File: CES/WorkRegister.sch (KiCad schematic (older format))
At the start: 12 parts, among them U401 RT1, U402 RT2, U403 RT3, U404 RT4, U405 BT1, U406 BT2

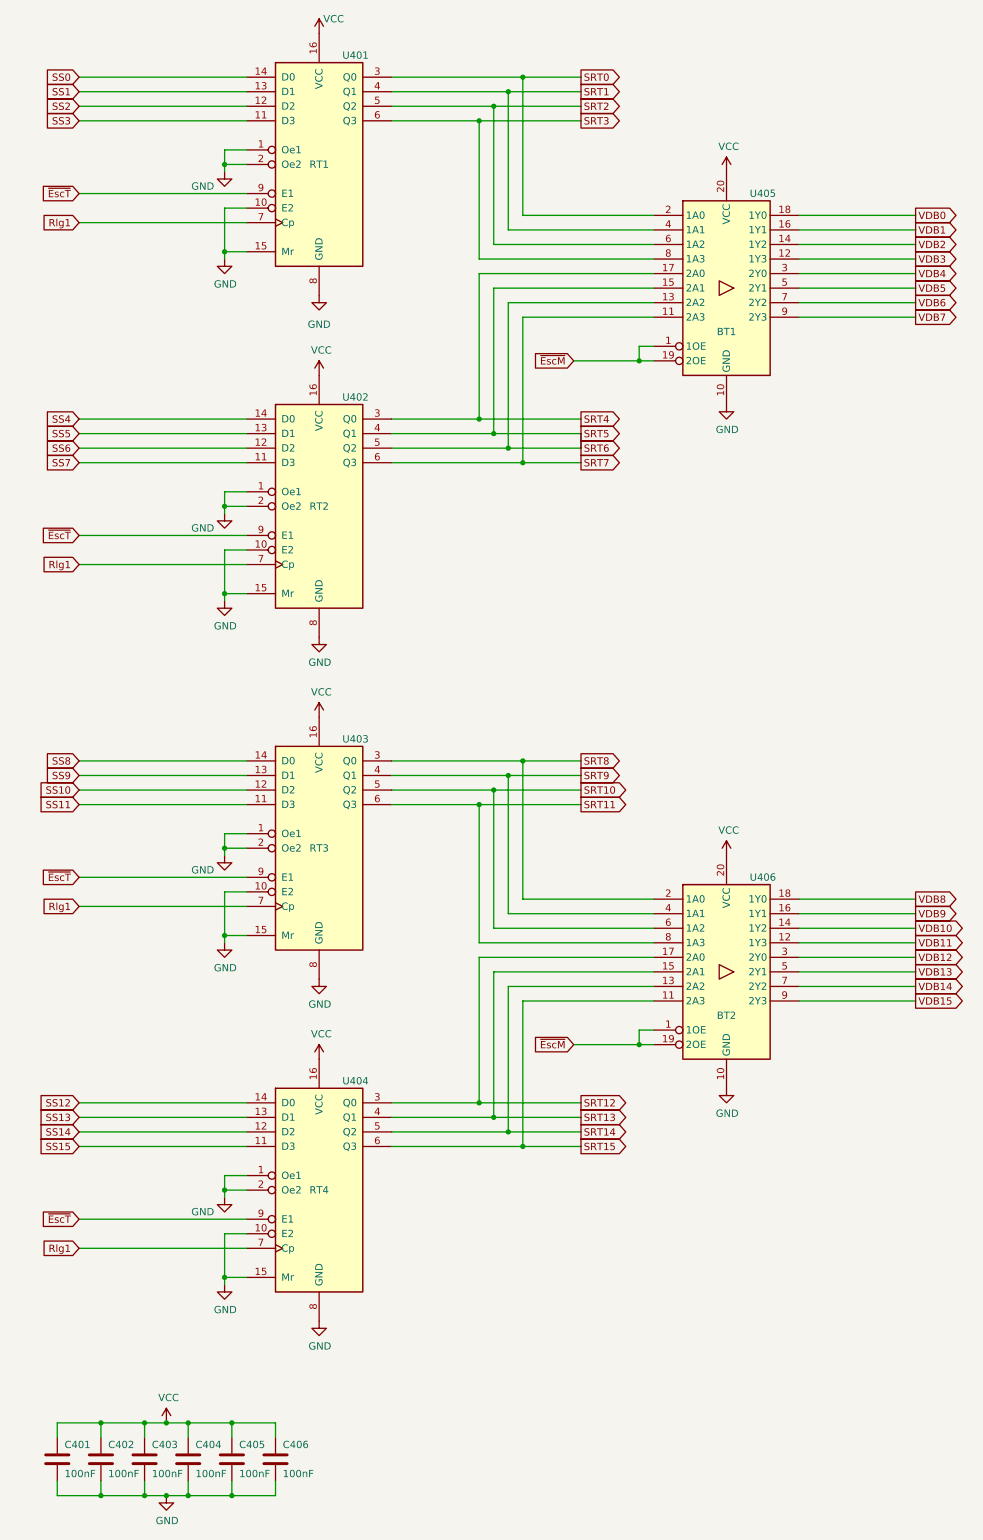
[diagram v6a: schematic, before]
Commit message: Correcting footprints errors
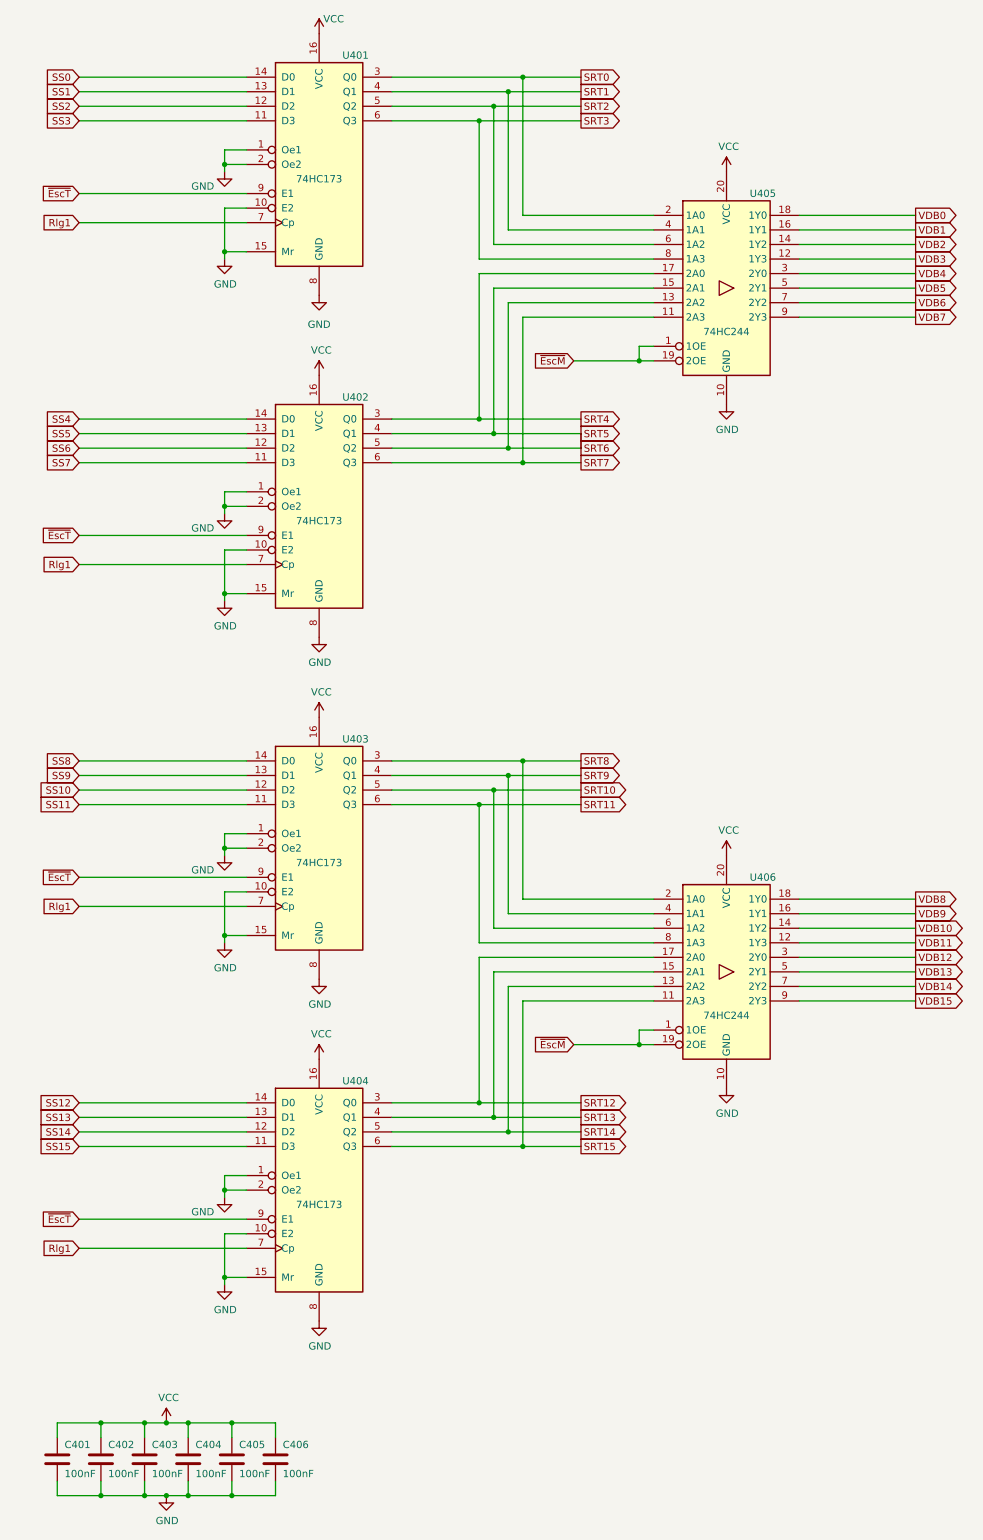
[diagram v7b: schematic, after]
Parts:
- C401, C402, C403, C404, C405, C406: footprint Capacitor_THT:CP_Radial_D5.0mm_P2.50mm -> Capacitor_THT:C_Disc_D4.3mm_W1.9mm_P5.00mm
- U401: value RT1 -> 74HC173
- U402: value RT2 -> 74HC173
- U403: value RT3 -> 74HC173
- U404: value RT4 -> 74HC173
- U405: value BT1 -> 74HC244
- U406: value BT2 -> 74HC244
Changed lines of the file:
@@
 P 5600 2450
 F 0 "U405" H 5850 3100 50  0000 C CNN
-F 1 "BT1" H 5600 2150 50  0000 C CNN
+F 1 "74HC244" H 5600 2150 50  0000 C CNN
 F 2 "Package_DIP:DIP-20_W7.62mm" H 5600 2450 50  0001 C CNN
 F 3 "https://assets.nexperia.com/documents/data-sheet/74HC_HCT244.pdf" H 5600 2450 50  0001 C CNN
@@
 P 5600 7150
 F 0 "U406" H 5850 7800 50  0000 C CNN
-F 1 "BT2" H 5600 6850 50  0000 C CNN
+F 1 "74HC244" H 5600 6850 50  0000 C CNN
 F 2 "Package_DIP:DIP-20_W7.62mm" H 5600 7150 50  0001 C CNN
 F 3 "https://assets.nexperia.com/documents/data-sheet/74HC_HCT244.pdf" H 5600 7150 50  0001 C CNN
@@
 F 0 "C401" H 1050 10600 50  0000 L CNN
 F 1 "100nF" H 1050 10400 50  0000 L CNN
-F 2 "Capacitor_THT:CP_Radial_D5.0mm_P2.50mm" H 1038 10350 50  0001 C CNN
+F 2 "Capacitor_THT:C_Disc_D4.3mm_W1.9mm_P5.00mm" H 1038 10350 50  0001 C CNN
 F 3 "~" H 1000 10500 50  0001 C CNN
 	1    1000 10500
@@
 F 0 "C402" H 1350 10600 50  0000 L CNN
 F 1 "100nF" H 1350 10400 50  0000 L CNN
-F 2 "Capacitor_THT:CP_Radial_D5.0mm_P2.50mm" H 1338 10350 50  0001 C CNN
+F 2 "Capacitor_THT:C_Disc_D4.3mm_W1.9mm_P5.00mm" H 1338 10350 50  0001 C CNN
 F 3 "~" H 1300 10500 50  0001 C CNN
 	1    1300 10500
@@
 F 0 "C403" H 1650 10600 50  0000 L CNN
 F 1 "100nF" H 1650 10400 50  0000 L CNN
-F 2 "Capacitor_THT:CP_Radial_D5.0mm_P2.50mm" H 1638 10350 50  0001 C CNN
+F 2 "Capacitor_THT:C_Disc_D4.3mm_W1.9mm_P5.00mm" H 1638 10350 50  0001 C CNN
 F 3 "~" H 1600 10500 50  0001 C CNN
 	1    1600 10500
@@
 F 0 "C404" H 1950 10600 50  0000 L CNN
 F 1 "100nF" H 1950 10400 50  0000 L CNN
-F 2 "Capacitor_THT:CP_Radial_D5.0mm_P2.50mm" H 1938 10350 50  0001 C CNN
+F 2 "Capacitor_THT:C_Disc_D4.3mm_W1.9mm_P5.00mm" H 1938 10350 50  0001 C CNN
 F 3 "~" H 1900 10500 50  0001 C CNN
 	1    1900 10500
@@
 F 0 "C405" H 2250 10600 50  0000 L CNN
 F 1 "100nF" H 2250 10400 50  0000 L CNN
-F 2 "Capacitor_THT:CP_Radial_D5.0mm_P2.50mm" H 2238 10350 50  0001 C CNN
+F 2 "Capacitor_THT:C_Disc_D4.3mm_W1.9mm_P5.00mm" H 2238 10350 50  0001 C CNN
 F 3 "~" H 2200 10500 50  0001 C CNN
 	1    2200 10500
@@
 F 0 "C406" H 2550 10600 50  0000 L CNN
 F 1 "100nF" H 2550 10400 50  0000 L CNN
-F 2 "Capacitor_THT:CP_Radial_D5.0mm_P2.50mm" H 2538 10350 50  0001 C CNN
+F 2 "Capacitor_THT:C_Disc_D4.3mm_W1.9mm_P5.00mm" H 2538 10350 50  0001 C CNN
 F 3 "~" H 2500 10500 50  0001 C CNN
 	1    2500 10500
@@
 P 2800 1600
 F 0 "U401" H 3050 2350 50  0000 C CNN
-F 1 "RT1" H 2800 1600 50  0000 C CNN
+F 1 "74HC173" H 2800 1500 50  0000 C CNN
 F 2 "Package_DIP:DIP-16_W7.62mm" H 2800 1600 50  0001 C CNN
 F 3 "http://www.ti.com/lit/gpn/cd74HC173" H 2800 1600 50  0001 C CNN
@@
 P 2800 3950
 F 0 "U402" H 3050 4700 50  0000 C CNN
-F 1 "RT2" H 2800 3950 50  0000 C CNN
+F 1 "74HC173" H 2800 3850 50  0000 C CNN
 F 2 "Package_DIP:DIP-16_W7.62mm" H 2800 3950 50  0001 C CNN
 F 3 "http://www.ti.com/lit/gpn/cd74HC173" H 2800 3950 50  0001 C CNN
@@
 P 2800 6300
 F 0 "U403" H 3050 7050 50  0000 C CNN
-F 1 "RT3" H 2800 6300 50  0000 C CNN
+F 1 "74HC173" H 2800 6200 50  0000 C CNN
 F 2 "Package_DIP:DIP-16_W7.62mm" H 2800 6300 50  0001 C CNN
 F 3 "http://www.ti.com/lit/gpn/cd74HC173" H 2800 6300 50  0001 C CNN
@@
 P 2800 8650
 F 0 "U404" H 3050 9400 50  0000 C CNN
-F 1 "RT4" H 2800 8650 50  0000 C CNN
+F 1 "74HC173" H 2800 8550 50  0000 C CNN
 F 2 "Package_DIP:DIP-16_W7.62mm" H 2800 8650 50  0001 C CNN
 F 3 "http://www.ti.com/lit/gpn/cd74HC173" H 2800 8650 50  0001 C CNN

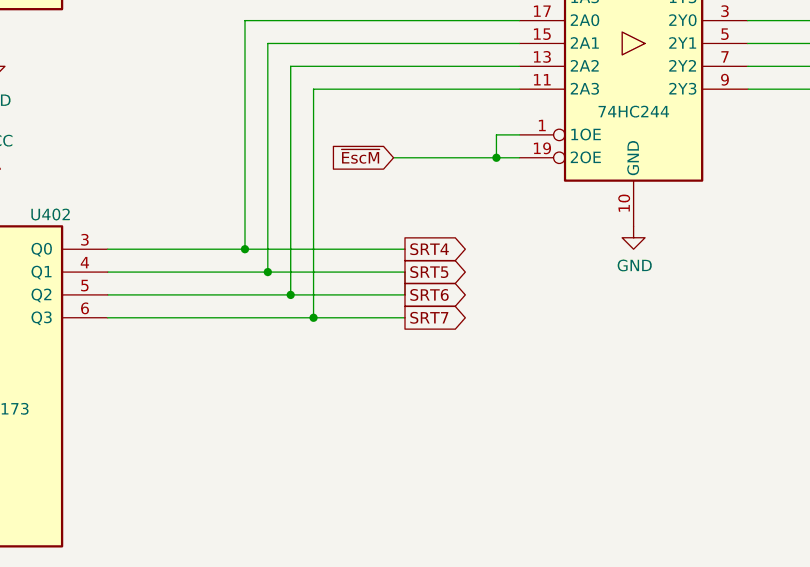
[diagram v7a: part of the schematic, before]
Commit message: All adders, registers and multiplexers in place
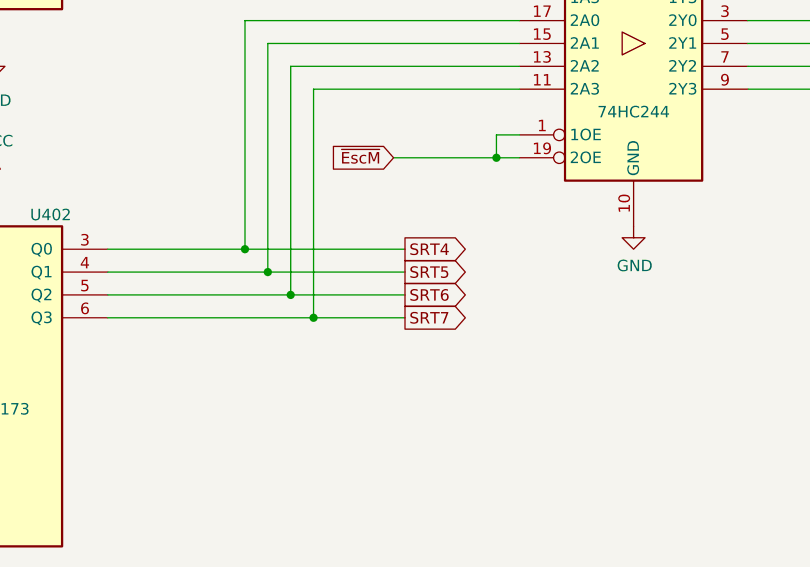
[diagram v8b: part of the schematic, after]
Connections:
- net SRT5: no longer U402.5 (Q2), U405.13 (2A2)
- new net SRT6: U402.5 (Q2), U405.13 (2A2)
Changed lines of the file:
@@
 	4100 3550 4600 3550
-Wire Wire Line
-	4600 3550 4600 3450
 Wire Wire Line
 	4600 3450 4000 3450
